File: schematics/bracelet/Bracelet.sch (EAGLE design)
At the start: 10 parts

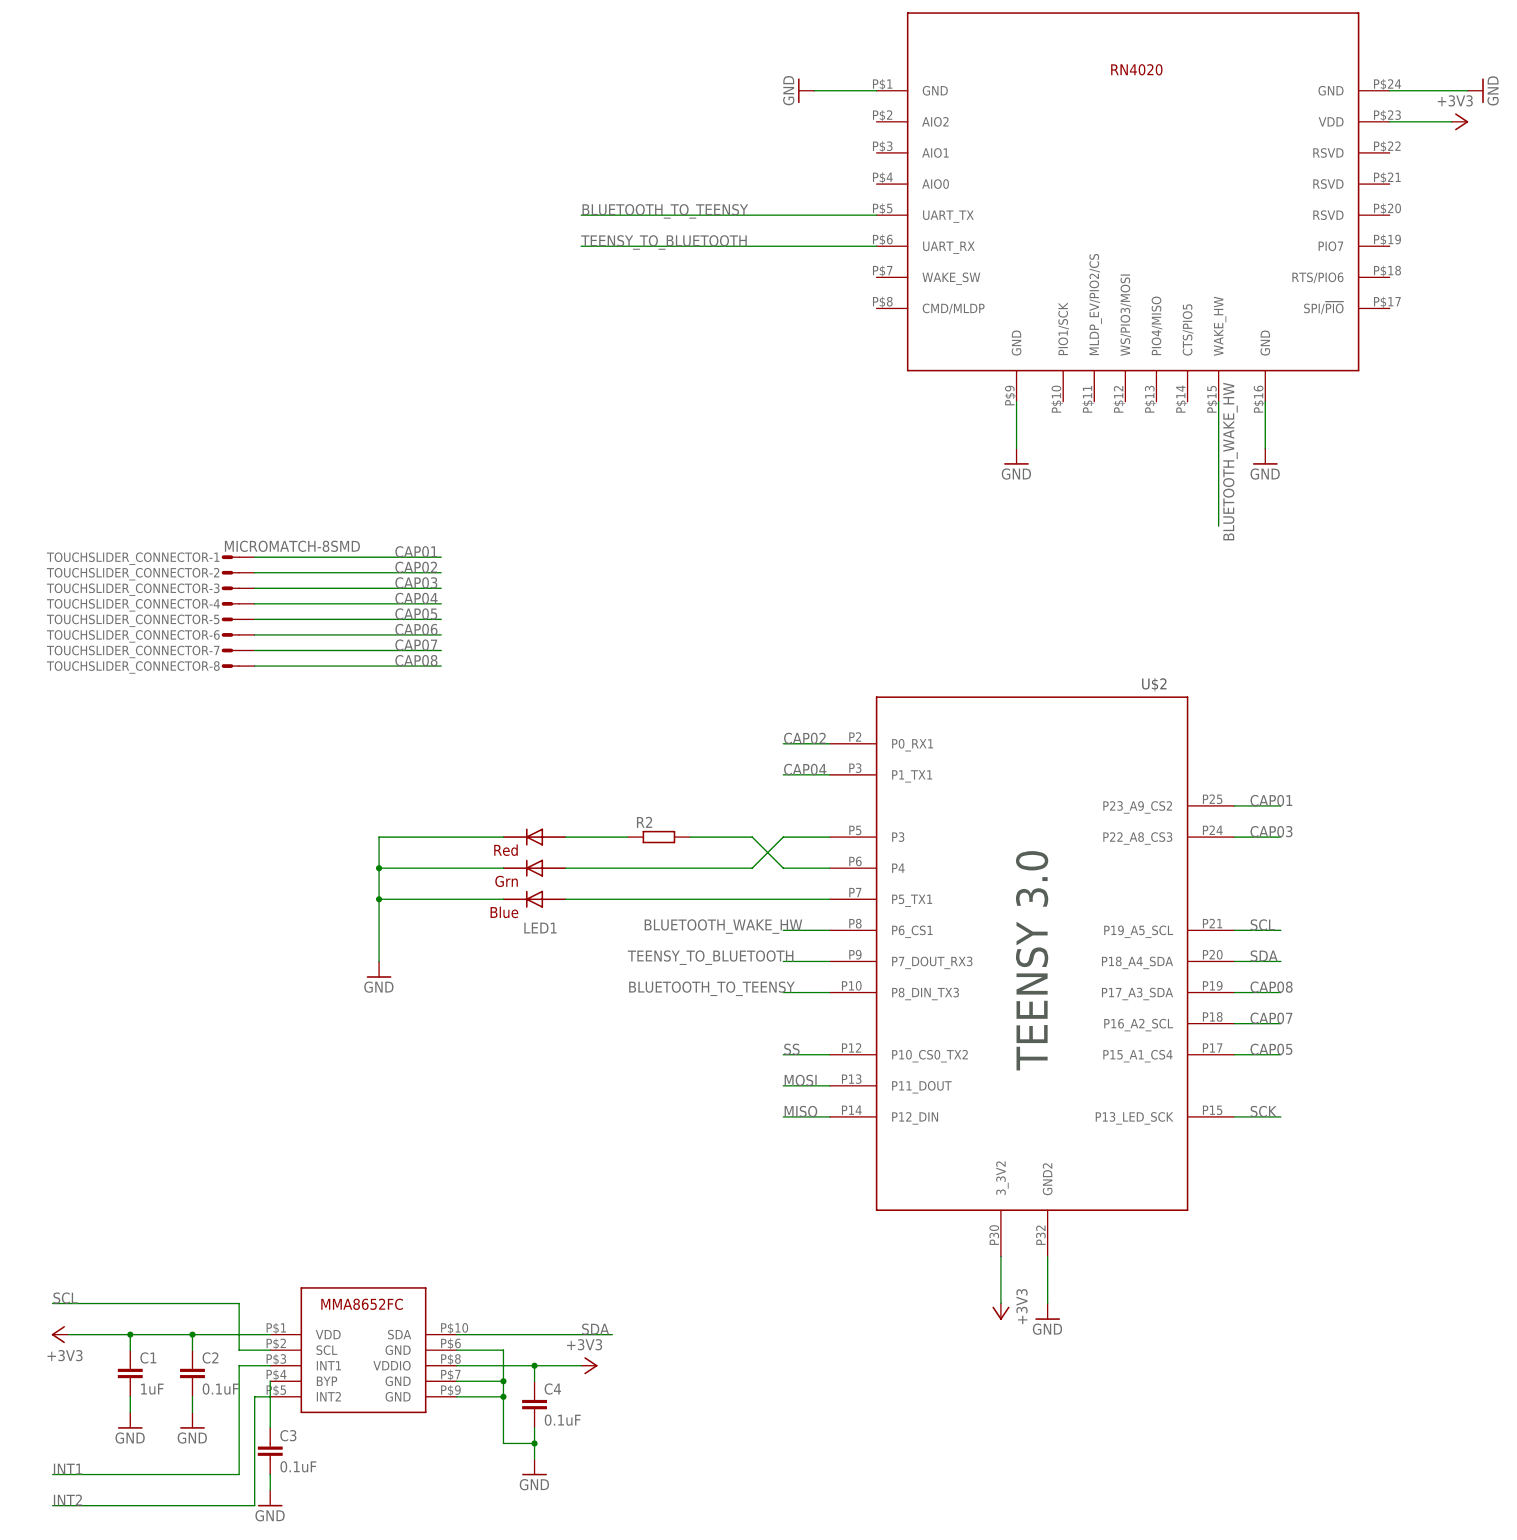
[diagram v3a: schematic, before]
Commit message: next revision for braclet board, now dual layer.
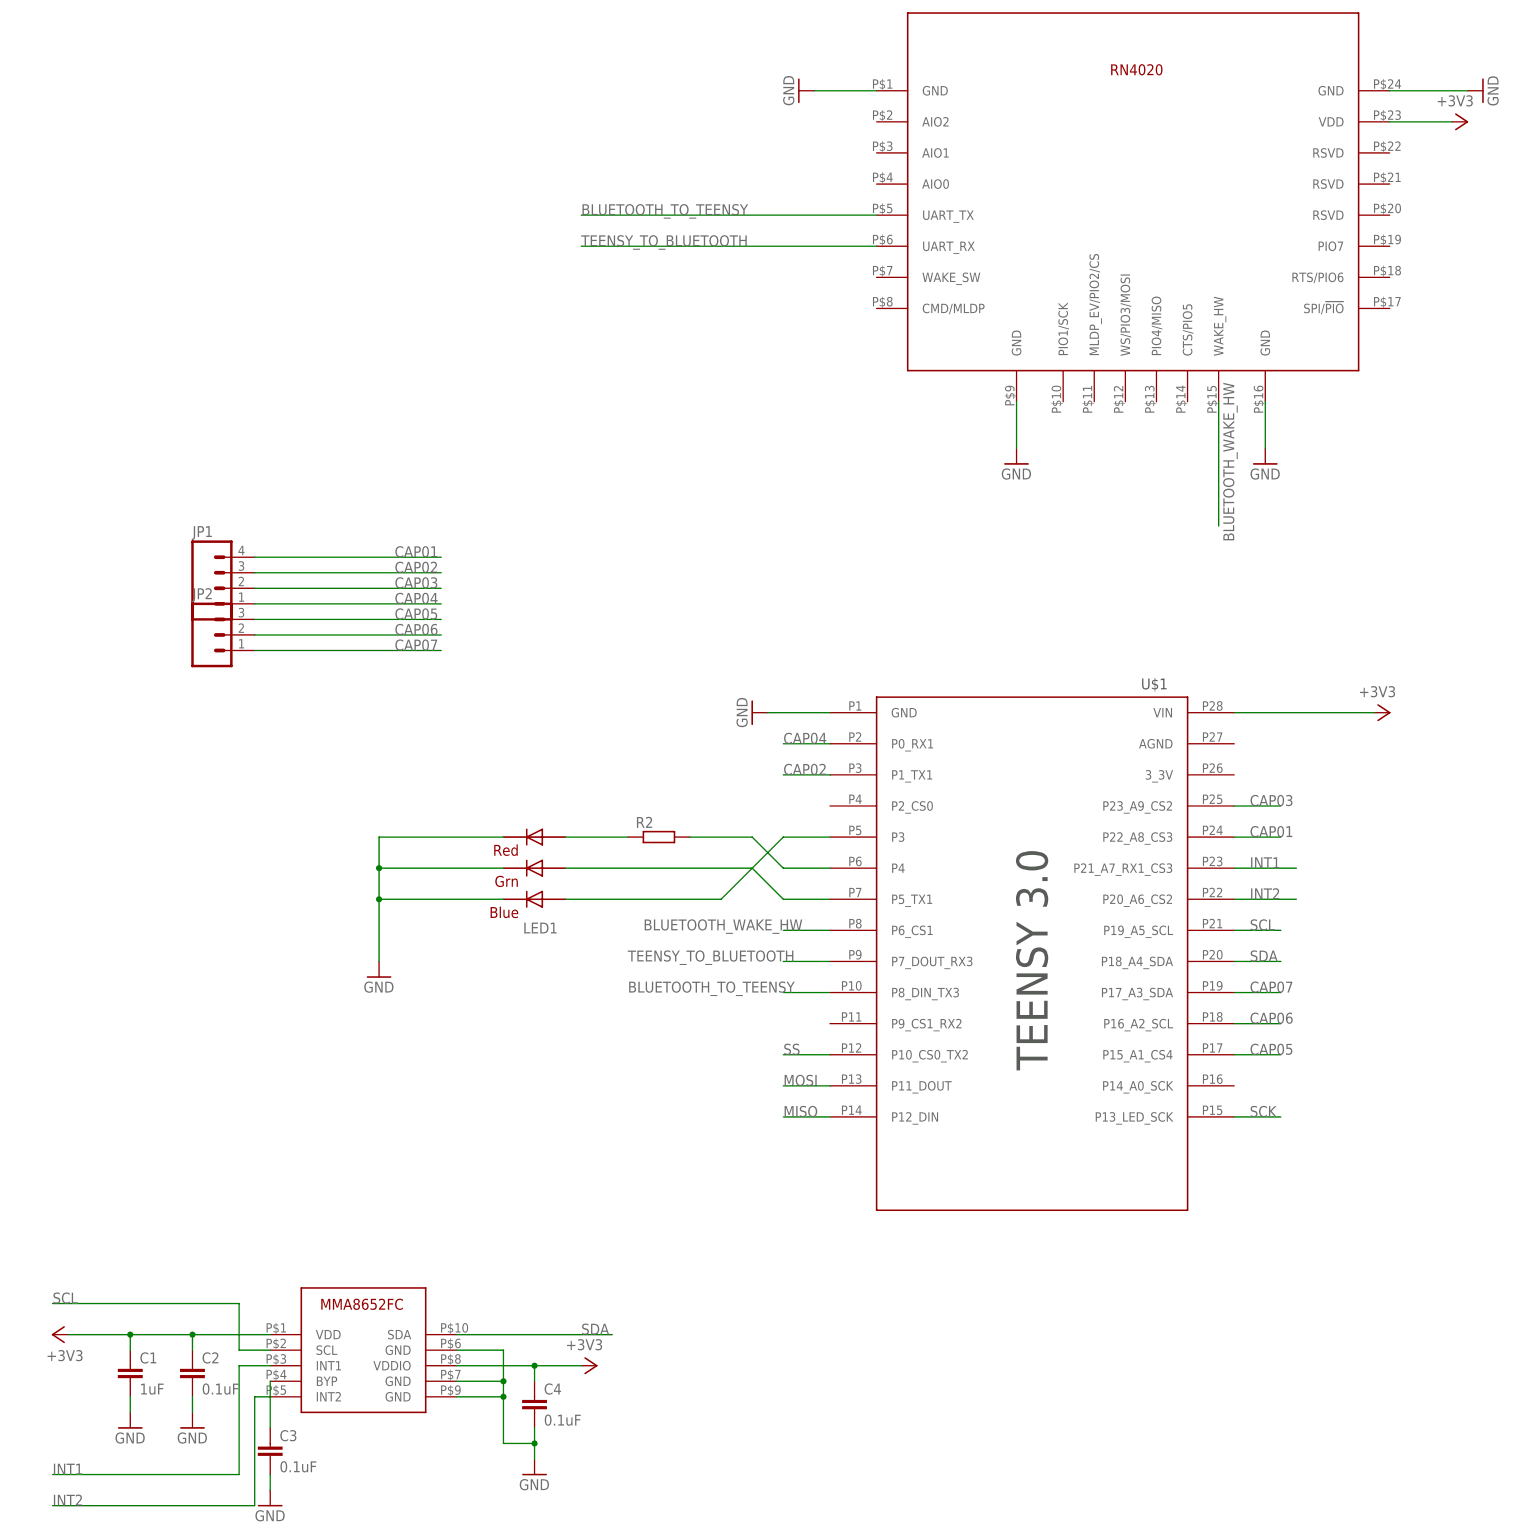
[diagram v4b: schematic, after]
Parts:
- removed TOUCHSLIDER_CONNECTOR: MICROMATCH-8SMD, con-amp-micromatch-smd:MICROMATCH-8SMD
- removed U$2: TEENSY3, teensy_minimal:TEENSY3
- added JP1: (no value), SparkFun-Connectors:M04PTH
- added JP2: (no value), SparkFun-Connectors:M03PTH
- added U$1: TEENSY3, teensy_base_compatible:TEENSY3
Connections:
- removed net CAP08: TOUCHSLIDER_CONNECTOR-8.S, U$2.P17_A3_SDA
- removed net N$3: LED1.BLUE_A, U$2.P5_TX1
- new net N$5: LED1.BLUE_A, U$1.P3
- net +3V3: now also U$1.VIN; no longer U$2.3_3V2
- net BLUETOOTH_TO_TEENSY: now also U$1.P8_DIN_TX3; no longer U$2.P8_DIN_TX3
- net BLUETOOTH_WAKE_HW: now also U$1.P6_CS1; no longer U$2.P6_CS1
- net CAP01: now also JP1.4, U$1.P22_A8_CS3; no longer TOUCHSLIDER_CONNECTOR-1.S, U$2.P23_A9_CS2
- net CAP02: now also JP1.3, U$1.P1_TX1; no longer TOUCHSLIDER_CONNECTOR-2.S, U$2.P0_RX1
- net CAP03: now also JP1.2, U$1.P23_A9_CS2; no longer TOUCHSLIDER_CONNECTOR-3.S, U$2.P22_A8_CS3
- net CAP04: now also JP1.1, U$1.P0_RX1; no longer TOUCHSLIDER_CONNECTOR-4.S, U$2.P1_TX1
- net CAP05: now also JP2.3, U$1.P15_A1_CS4; no longer TOUCHSLIDER_CONNECTOR-5.S, U$2.P15_A1_CS4
- net CAP06: now also JP2.2, U$1.P16_A2_SCL; no longer TOUCHSLIDER_CONNECTOR-6.S
- net CAP07: now also JP2.1, U$1.P17_A3_SDA; no longer TOUCHSLIDER_CONNECTOR-7.S, U$2.P16_A2_SCL
- net GND: now also U$1.GND; no longer U$2.GND2
- net INT1: now also U$1.P21_A7_RX1_CS3
- net INT2: now also U$1.P20_A6_CS2
- net MISO: now also U$1.P12_DIN; no longer U$2.P12_DIN
- net MOSI: now also U$1.P11_DOUT; no longer U$2.P11_DOUT
- net N$4: now also U$1.P4; no longer U$2.P4
- net N$6: now also U$1.P5_TX1; no longer U$2.P3
- net SCK: now also U$1.P13_LED_SCK; no longer U$2.P13_LED_SCK
- net SCL: now also U$1.P19_A5_SCL; no longer U$2.P19_A5_SCL
- net SDA: now also U$1.P18_A4_SDA; no longer U$2.P18_A4_SDA
- net SS: now also U$1.P10_CS0_TX2; no longer U$2.P10_CS0_TX2
- net TEENSY_TO_BLUETOOTH: now also U$1.P7_DOUT_RX3; no longer U$2.P7_DOUT_RX3
